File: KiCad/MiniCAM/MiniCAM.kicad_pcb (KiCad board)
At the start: 4 copper layers, 25.4 x 25.4 mm, 64 parts, among them J1 SMA-J-P-H-RA-TH1, J2 Conn_01x02, J3 Conn_01x03, U1 NCV8154MW180280TBG, U2 DS90UB933-Q1, U3 MT9P031, U4 SiT_2.5mmx2mm

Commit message: Finish initial schematic, layout, and routing.
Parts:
- added C36: 10uF, .Capacitor:C_0603_1608Metric_L, F.Cu at (108.0, 47.1)
- added J4: Conn_02x03_Odd_Even, Connector_PinSocket_1.27mm:PinSocket_2x03_P1.27mm_Horizontal, F.Cu at (119.9, 45.9)
- C11, C16: value C_Small -> 1uF
- C12: value 1uF -> 10uF; footprint .Capacitor:C_0402_1005Metric_L -> .Capacitor:C_0603_1608Metric_L
- C17: value C_Small -> 10uF; footprint .Capacitor:C_0402_1005Metric_L -> .Capacitor:C_0603_1608Metric_L
- C18, C21, C26, C29, C31: value C_Small -> 10nF
- C19, C22, C27, C30, C32: value C_Small -> 0.1uF
- C20, C23, C28: value C_Small -> 4.7uF
- C35: value ?? -> 1uF
- J2, J3: moved to B.Cu
- R7, R8: value ?? -> 10K
- R9: value ?? -> 100K
- moved D1 63.7 mm to (102.8, 38.1), turned to 270 degrees
- moved R10 55.4 mm to (102.8, 45.3), turned to 270 degrees
- moved C16 53.2 mm to (106.9, 46.8), turned to 270 degrees
- moved R6 52.6 mm to (105.6, 39.2), turned to 270 degrees
- moved J2 52.2 mm to (114.2, 48.9), turned to 270 degrees
- moved C31 50.9 mm to (104.6, 37.4), turned to 90 degrees
- moved R5 50.8 mm to (104.7, 39.2), turned to 270 degrees
- moved C30 50.8 mm to (107.9, 33.3), turned to 90 degrees
- moved R2 49.3 mm to (102.8, 35.9), turned to 270 degrees
- moved C14 48.8 mm to (109.3, 33.7), turned to 180 degrees
- moved U4 48.5 mm to (104.8, 44.9)
- moved C34 48.3 mm to (104.2, 43.1)
- moved J3 48.0 mm to (116.8, 27.1), turned to 90 degrees
- moved R8 47.5 mm to (113.7, 46.3), turned to 180 degrees
- moved C25 46.6 mm to (114.6, 38.7)
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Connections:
- net Net-(U2-Pad19) renamed /DIN0
- net Net-(U2-Pad20) renamed /DIN1
- net Net-(U2-Pad21) renamed /DIN2
- net Net-(U2-Pad22) renamed /DIN3
- net Net-(U2-Pad23) renamed /DIN4
- net Net-(U2-Pad24) renamed /DIN5
- net Net-(U2-Pad26) renamed /DIN6
- net Net-(U2-Pad27) renamed /DIN7
- net Net-(U2-Pad29) renamed /DIN8
- net Net-(U2-Pad30) renamed /DIN9
- C17 pad 1: +1V8 -> +2V8
- J2 pad 1: Net-(J2-Pad1) -> /SCL
- J2 pad 2: Net-(J2-Pad2) -> /SDA
- J3 pad 1: Net-(J3-Pad1) -> GND
- J3 pad 2: Net-(J3-Pad2) -> +5V
- J3 pad 3: Net-(J3-Pad3) -> +2V8
- L3 pad 2: Net-(L3-Pad2) -> /VDDT
- L4 pad 2: Net-(L4-Pad2) -> /VDDPLL
- L5 pad 2: Net-(L5-Pad2) -> /VDDCML
- U1 pad 11: (no net) -> GND
- U3 pad 4: /SCK -> /SCL
- U4 pad 1: Net-(U4-Pad1) -> Net-(R10-Pad2)
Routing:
- net +1V8: track 0.00 -> 73.8 mm, vias 0 -> 8
- net GND: track 0.00 -> 60.9 mm, vias 0 -> 39
- net /SDA: track 0.00 -> 37.9 mm, vias 0 -> 1
- net +5V: track 0.00 -> 36.4 mm, vias 0 -> 6
- net +2V8: track 0.00 -> 33.8 mm, vias 0 -> 13
- net /SCL: track 0.00 -> 30.8 mm, vias 0 -> 2
- net /GPO3: track 0.00 -> 26.5 mm, vias 0 -> 1
- net /GPO0: track 0.00 -> 26.1 mm, vias 0 -> 1
- net /GPO2: track 0.00 -> 24.4 mm, vias 0 -> 1
- net /GPO1: track 0.00 -> 24.1 mm, vias 0 -> 1
- net /nRESET: track 0.00 -> 11.7 mm, vias 0 -> 1
- net /DIN9: track 0.00 -> 11.4 mm, vias 0 -> 1
- net /LV: track 0.00 -> 11.1 mm, vias 0 -> 1
- net /PDB: track 0.00 -> 10.7 mm
- net /FV: track 0.00 -> 10.3 mm, vias 0 -> 1
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- added copper zone on F.Cu, net +1V8
- added copper zone on F.Cu, net +2V8
- added copper zone on B.Cu, net +5V
- added copper zone on F.Cu, net +5V
- added copper zone on B.Cu, net GND
- added copper zone on F.Cu, net GND
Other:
- outline, holes or cut-outs redrawn
- board text added: "5MP"
- board text added: "5V"
- board text added: "Aharoni Lab 07/17/2020"
- board text added: "GND"
- board text added: "GND 5V VIO"
- board text added: "MT9P031"
- board text added: "MiniCAM"
- board text added: "SCL"
- board text added: "SDA"
- board text added: "v0.1"

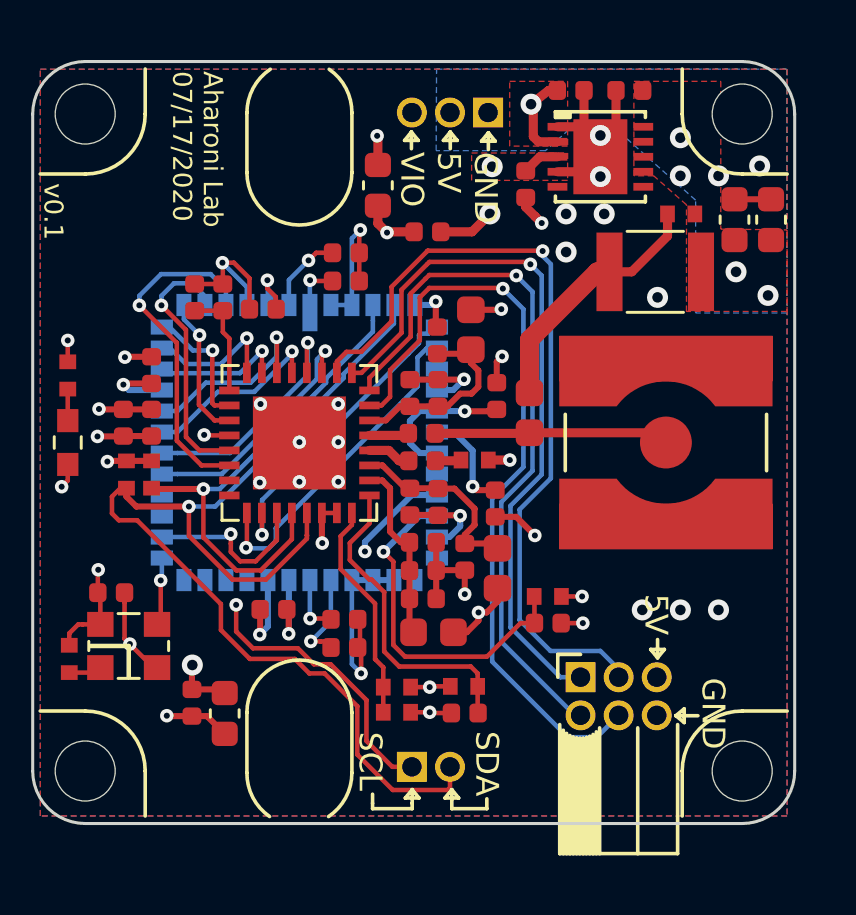
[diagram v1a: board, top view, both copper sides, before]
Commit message: Switch 2 and 3 socket headers for longer 3D model ones. Generate new STEP.
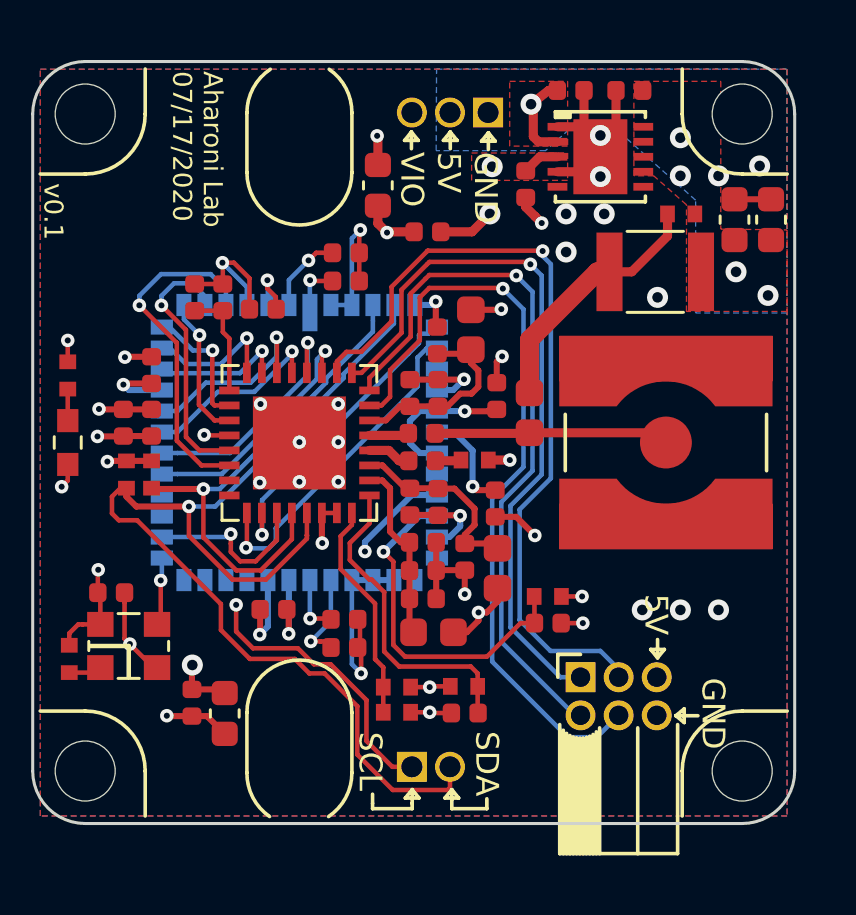
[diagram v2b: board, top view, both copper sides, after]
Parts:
- J2: footprint Connector_PinHeader_1.27mm:PinHeader_1x02_P1.27mm_Vertical -> Connector_PinSocket_1.27mm:PinSocket_1x02_P1.27mm_Vertical
- J3: footprint Connector_PinHeader_1.27mm:PinHeader_1x03_P1.27mm_Vertical -> Connector_PinSocket_1.27mm:PinSocket_1x03_P1.27mm_Vertical

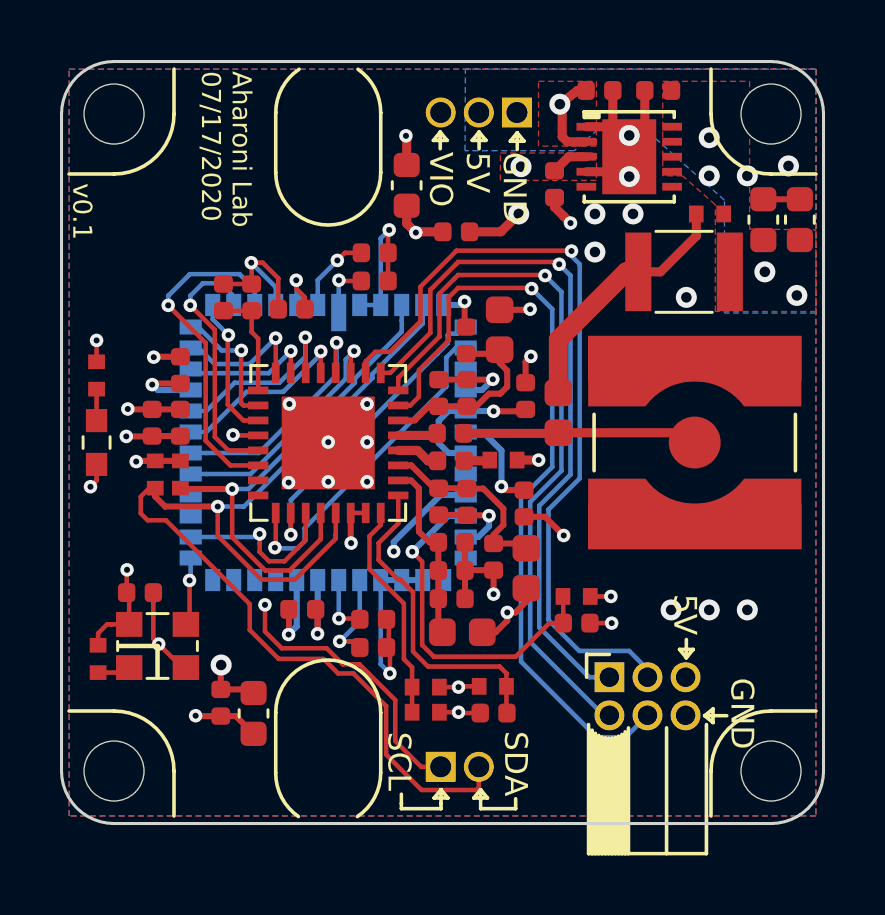
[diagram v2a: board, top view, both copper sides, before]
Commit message: Move LED ring headers to a consistent 4mm x 1mm spacing from center on lens.
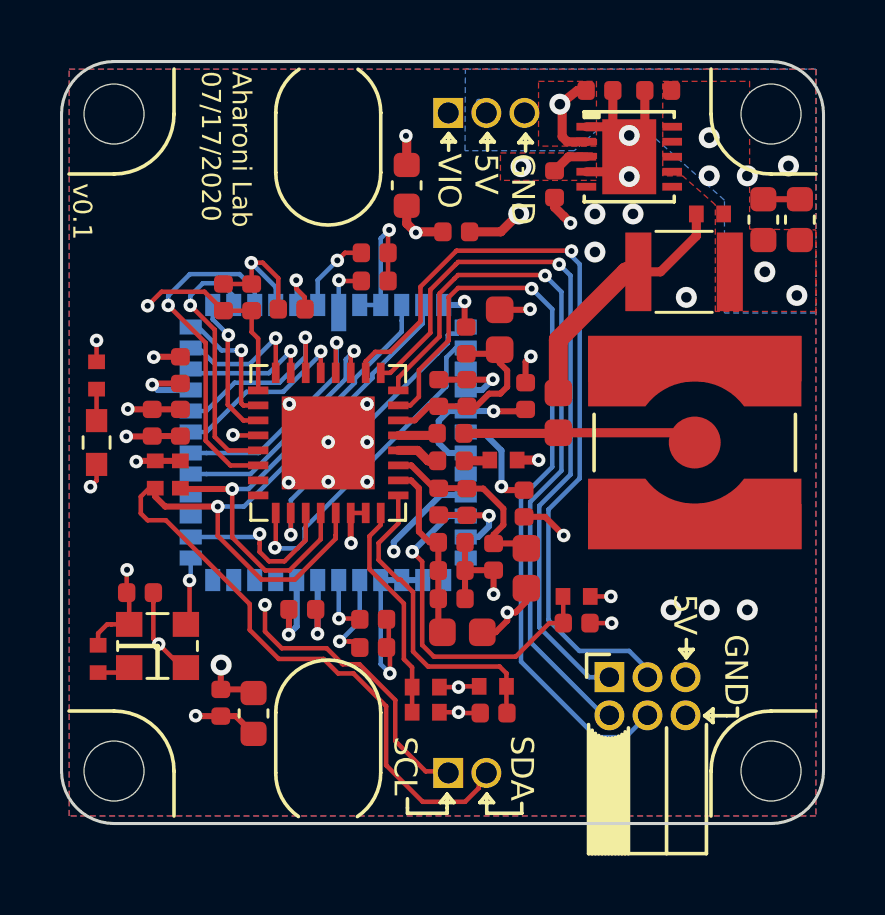
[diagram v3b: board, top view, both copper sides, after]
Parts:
- moved J3 2.29 mm to (114.5, 27.1), turned to 270 degrees
- moved J2 0.32 mm to (114.5, 49.1)
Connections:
- J3 pad 1: GND -> +2V8
- J3 pad 3: +2V8 -> GND
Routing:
- net +2V8: track 33.8 -> 36.8 mm, vias 13 -> 14
- net +5V: track 36.4 -> 37.4 mm
- net /SDA: track 37.9 -> 38.5 mm

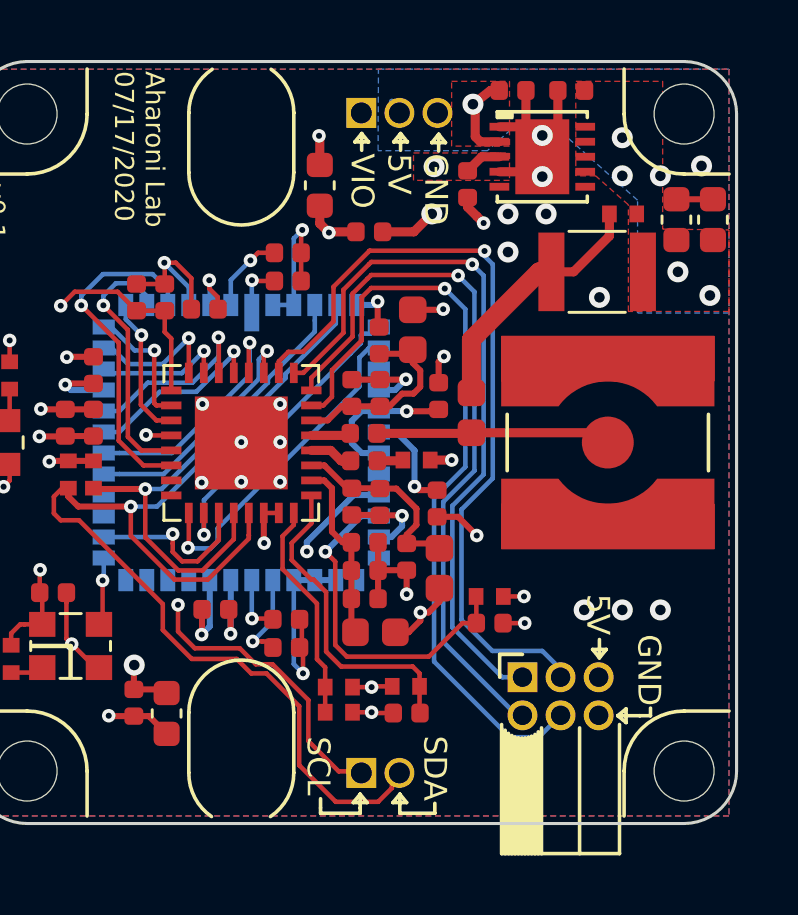
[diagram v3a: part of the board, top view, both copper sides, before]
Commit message: Updated LED ring PCB Board
Changed 10UF 0603 to 1210 50V: C1210C106K5RACTU
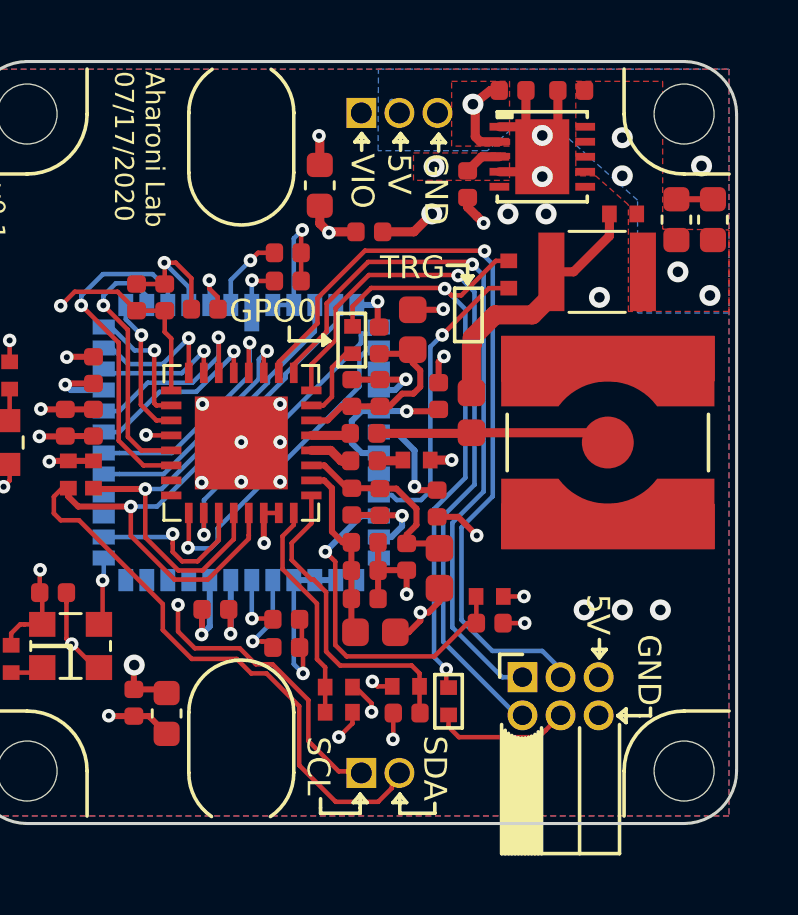
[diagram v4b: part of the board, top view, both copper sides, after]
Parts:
- added R11: 0, .Resistor:R_0402_1005Metric_ERJ_L, F.Cu at (119.4, 32.5)
- added R12: 0, .Resistor:R_0402_1005Metric_ERJ_L, F.Cu at (117.4, 46.7)
- added R13: 0, .Resistor:R_0402_1005Metric_ERJ_L, F.Cu at (114.2, 34.7)
- R5, R6: value 1K -> 2K
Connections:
- J4 pad 4: /GPO0 -> Net-(J4-Pad4)
- R8 pad 1: +2V8 -> +1V8
- U2 pad 15: /GPO0 -> Net-(R13-Pad1)
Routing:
- net /TRIGGER: track 3.37 -> 10.2 mm
- net /GPO0: track 26.1 -> 20.9 mm, vias 1 -> 2
- net Net-(J4-Pad4): track 0.00 -> 4.58 mm
- net +1V8: track 74.3 -> 78.7 mm, vias 8 -> 9
- net Net-(R13-Pad1): track 0.00 -> 2.66 mm
- net +2V8: track 36.8 -> 36.2 mm
- net GND: track 60.9 -> 61.4 mm
- net +5V: vias 6 -> 5
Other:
- board text added: "GPO0"
- board text added: "TRG"

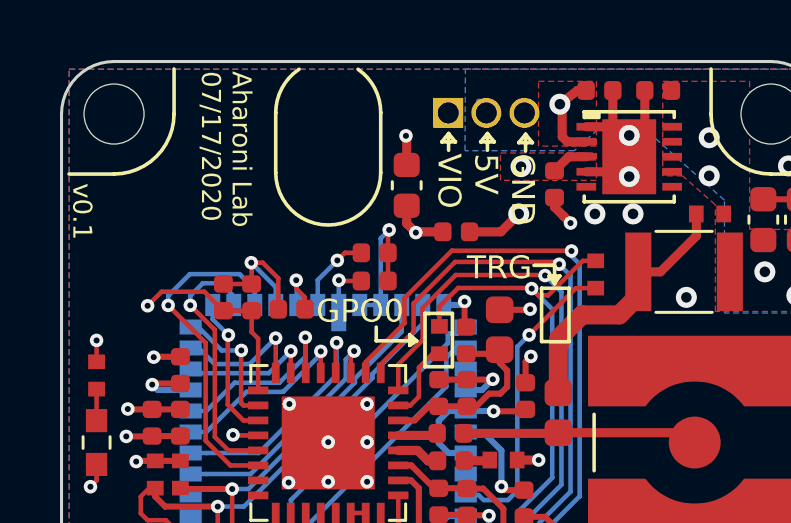
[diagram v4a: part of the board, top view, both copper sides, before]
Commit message: Correct minor error on top silk screen. Change to rev v1.0
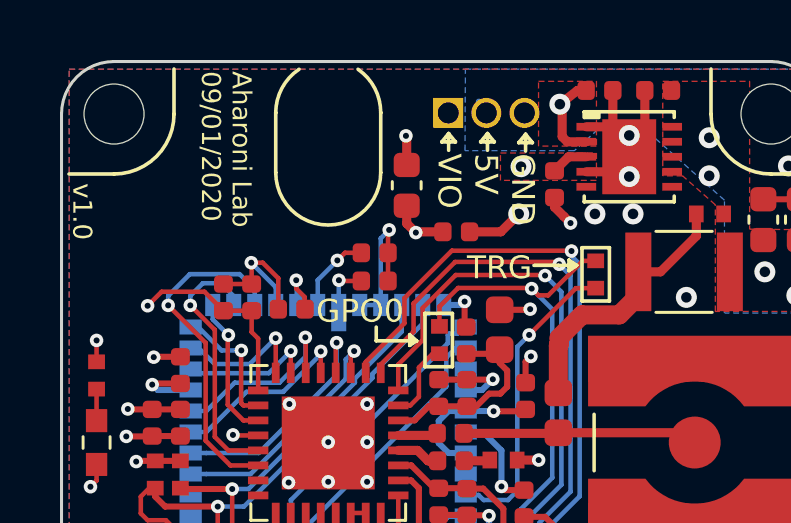
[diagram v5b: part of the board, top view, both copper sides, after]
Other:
- board text added: "Aharoni Lab 09/01/2020"
- board text added: "v1.0"
- board text removed: "Aharoni Lab 07/17/2020"
- board text removed: "v0.1"
